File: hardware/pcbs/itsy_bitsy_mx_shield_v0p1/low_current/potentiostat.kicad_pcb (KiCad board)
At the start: 2 copper layers, 144.8 x 88.9 mm, 139 parts, among them K1 Conn_01x03, P1 Conn_01x02, P10 Conn_01x02, P11 Conn_01x02, P12 Conn_01x02, P13 Conn_02x05_Odd_Even, P14 Conn_02x05_Odd_Even, P15 Conn_02x02_Odd_Even, P16 Conn_02x02_Odd_Even, P17 Conn_01x02, P18 Conn_01x02, P19 Conn_01x02, P2 Conn_01x02, P20 Conn_01x02, P21 Conn_01x02, P22 Conn_01x02, P3 Conn_01x02, P4 Conn_01x02, P5 Conn_01x02, P6 Conn_01x02, P7 Conn_01x02, P8 Conn_01x02, P9 Conn_01x02, U1 74HC138, U11 OP07, U12 OP07, U13 OP07, U14 OP07, U15 OP07, U16 OP07, U17 OP07, U18 OP07, U19 74HC138, U2 ITSY_BITSY_M4, U20 OP07, U21 74HC138, U3 DG411xY, U4 DG411xY, U5 DG411xY, U6 MEA1D05XXSC, U7 DG411xY, U8 DG411xY, U9 TL072

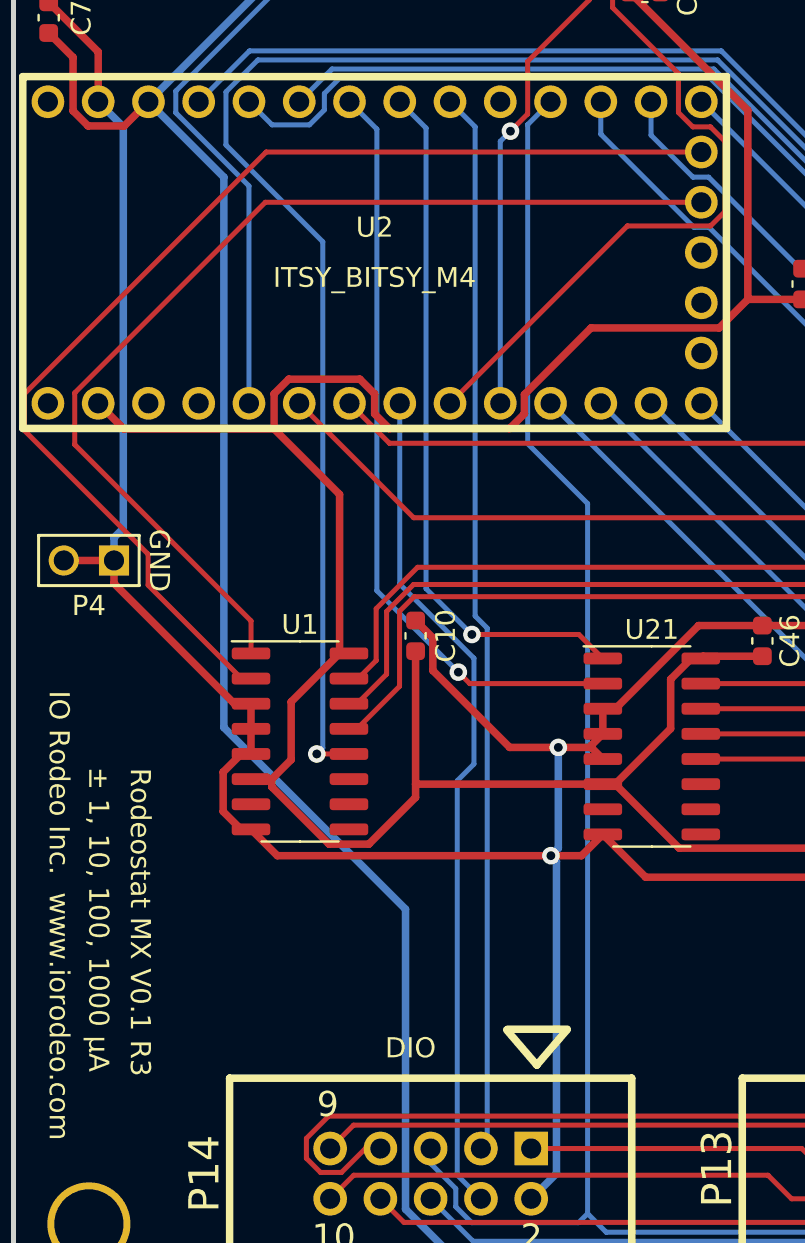
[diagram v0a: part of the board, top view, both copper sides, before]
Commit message: Added fab files to include through hole assembly.
Increased revision number V0.1 R4.  Remade gerbers to include addtional
elements on silkscreen.
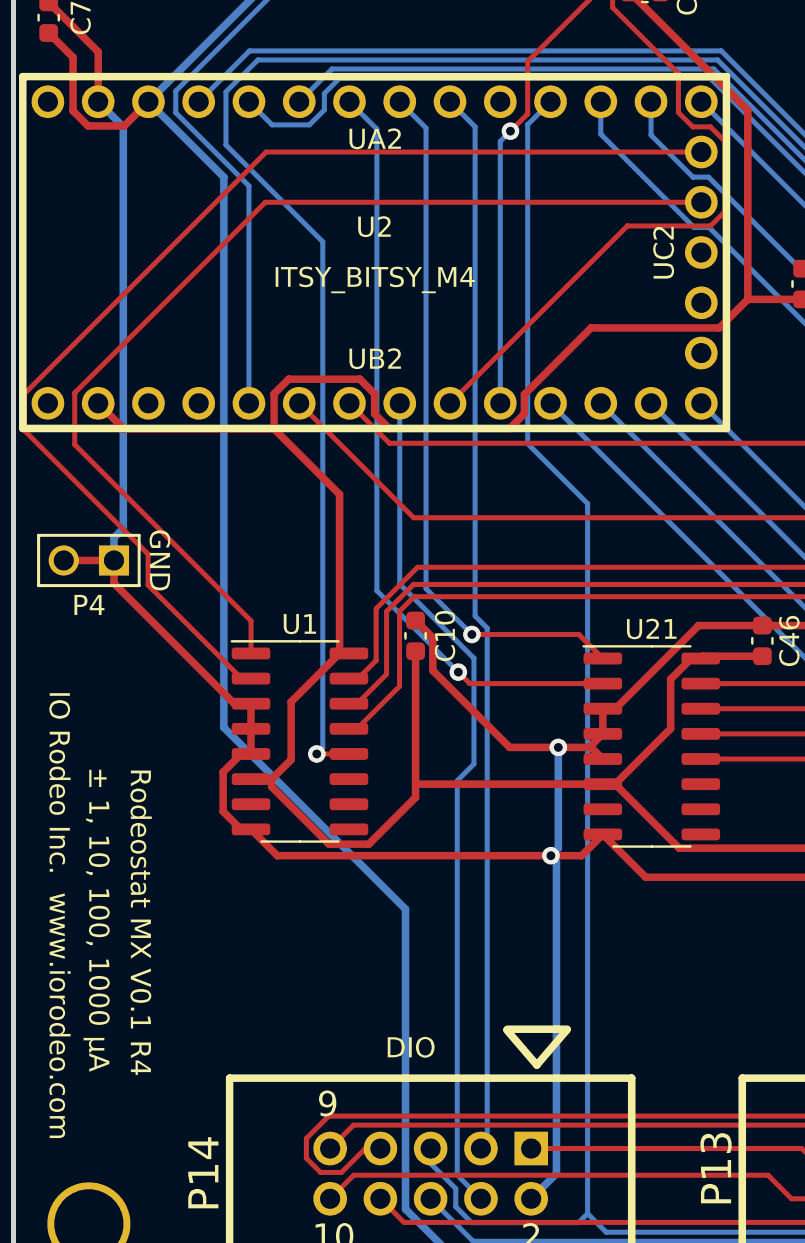
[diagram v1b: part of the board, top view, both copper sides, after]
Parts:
- added UA2: header_14_pos, dummy:header_14_pos, F.Cu at (69.0, 79.2)
- added UB2: header_14_pos, dummy:header_14_pos, F.Cu at (69.0, 94.4)
- added UC2: header_5_pos, dummy:header_5_pos, F.Cu at (85.6, 86.8)
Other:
- board text added: "Rodeostat MX V0.1 R4"
- board text removed: "Rodeostat MX V0.1 R3"
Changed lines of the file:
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@@
     (tracks 1443)
     (zones 0)
-    (modules 139)
+    (modules 142)
     (nets 133)
   )
@@
     (46 B.CrtYd user)
     (47 F.CrtYd user)
+    (49 F.Fab user)
   )
   (setup
@@
       (drillshape 0)
       (scaleselection 1)
-      (outputdirectory "gerber_v0p1_r3/"))
+      (outputdirectory "gerber_v0p1_r4/"))
   )
   (net 0 "")
@@
     (descr "Connecteur 3 pins")
     (tags "CONN DEV")
+    (attr smd)
     (fp_text reference K1 (at 5.08 -0.254 270) (layer F.SilkS)
       (effects (font (size 1.016 1.016) (thickness 0.2032)))
@@
   (module 5x2_shrd_header:5X2_SHRD_HEADER (layer F.Cu)
     (at 71.882 133.35 180)
+    (attr smd)
     (fp_text reference P14 (at 11.43 0 270) (layer F.SilkS)
       (effects (font (size 1.524 1.524) (thickness 0.3048)))
@@
   (module 5x2_shrd_header:5X2_SHRD_HEADER (layer F.Cu)
     (at 97.79 133.35 180)
+    (attr smd)
     (fp_text reference P13 (at 11.43 0.254 270) (layer F.SilkS)
       (effects (font (size 1.524 1.524) (thickness 0.3048)))
@@
     (descr "Double rangee de contacts 2 x 2 pins")
     (tags CONN)
+    (attr smd)
     (fp_text reference P16 (at -3.556 0 90) (layer F.SilkS)
       (effects (font (size 1.016 1.016) (thickness 0.2032)))
@@
     (descr "Double rangee de contacts 2 x 2 pins")
     (tags CONN)
+    (attr smd)
     (fp_text reference P15 (at -3.556 0 90) (layer F.SilkS)
       (effects (font (size 1.016 1.016) (thickness 0.2032)))
@@
   (module MEA1:MEA1 (layer F.Cu)
     (at 70.358 54.102)
+    (attr smd)
     (fp_text reference U6 (at -9.652 1.016 90) (layer F.SilkS)
       (effects (font (size 1.016 1.016) (thickness 0.2032)))
@@
   (module ost_connblocks:CONNBLOCK2 (layer F.Cu)
     (at 189.23 71.12 270)
+    (attr smd)
     (fp_text reference P1 (at 0.508 4.826 90) (layer F.SilkS)
       (effects (font (size 1.524 1.524) (thickness 0.3048)))
@@
   (module ost_connblocks:CONNBLOCK2 (layer F.Cu)
     (at 189.23 82.55 270)
+    (attr smd)
     (fp_text reference P2 (at 0.508 4.826 90) (layer F.SilkS)
       (effects (font (size 1.524 1.524) (thickness 0.3048)))
@@
   (module ost_connblocks:CONNBLOCK2 (layer F.Cu)
     (at 189.23 93.98 270)
+    (attr smd)
     (fp_text reference P3 (at 0.508 4.826 90) (layer F.SilkS)
       (effects (font (size 1.524 1.524) (thickness 0.3048)))
@@
       (net 10 /GND))
   )
+  (module dummy:header_14_pos (layer F.Cu)
+    (at 69.05 79.179999)
+    (attr smd)
+    (fp_text reference UA2 (at 0.038 1.909501) (layer F.SilkS)
+      (effects (font (size 1.016 1.016) (thickness 0.2032)))
+    )
+    (fp_text value header_14_pos (at 0.127 -1.651) (layer F.Fab) hide
+      (effects (font (size 1 1) (thickness 0.15)))
+    )
+    (fp_circle (center 16.51 0) (end 17.018 0) (layer F.Fab) (width 0.15))
+    (fp_circle (center 13.97 0) (end 14.478 0) (layer F.Fab) (width 0.15))
+    (fp_circle (center 11.43 0) (end 11.938 0) (layer F.Fab) (width 0.15))
+    (fp_circle (center 8.89 0) (end 9.398 0) (layer F.Fab) (width 0.15))
+    (fp_circle (center -16.51 0) (end -16.002 0) (layer F.Fab) (width 0.15))
+    (fp_circle (center -13.97 0) (end -13.462 0) (layer F.Fab) (width 0.15))
+    (fp_circle (center -11.43 0) (end -10.922 0) (layer F.Fab) (width 0.15))
+    (fp_circle (center -8.89 0) (end -8.382 0) (layer F.Fab) (width 0.15))
+    (fp_circle (center 6.35 0) (end 6.858 0) (layer F.Fab) (width 0.15))
+    (fp_circle (center -6.35 0) (end -5.842 0) (layer F.Fab) (width 0.15))
+    (fp_circle (center 3.81 0) (end 4.318 0) (layer F.Fab) (width 0.15))
+    (fp_circle (center 1.27 0) (end 1.778 0) (layer F.Fab) (width 0.15))
+    (fp_circle (center -3.81 0) (end -3.302 0) (layer F.Fab) (width 0.15))
+    (fp_circle (center -1.27 0) (end -0.762 0) (layer F.Fab) (width 0.15))
+  )
+  (module dummy:header_14_pos (layer F.Cu)
+    (at 69.05 94.41942)
+    (attr smd)
+    (fp_text reference UB2 (at 0.038 -2.21742) (layer F.SilkS)
+      (effects (font (size 1.016 1.016) (thickness 0.2032)))
+    )
+    (fp_text value header_14_pos (at 0.127 -1.651) (layer F.Fab) hide
+      (effects (font (size 1 1) (thickness 0.15)))
+    )
+    (fp_circle (center -1.27 0) (end -0.762 0) (layer F.Fab) (width 0.15))
+    (fp_circle (center -3.81 0) (end -3.302 0) (layer F.Fab) (width 0.15))
+    (fp_circle (center 1.27 0) (end 1.778 0) (layer F.Fab) (width 0.15))
+    (fp_circle (center 3.81 0) (end 4.318 0) (layer F.Fab) (width 0.15))
+    (fp_circle (center -6.35 0) (end -5.842 0) (layer F.Fab) (width 0.15))
+    (fp_circle (center 6.35 0) (end 6.858 0) (layer F.Fab) (width 0.15))
+    (fp_circle (center -8.89 0) (end -8.382 0) (layer F.Fab) (width 0.15))
+    (fp_circle (center -11.43 0) (end -10.922 0) (layer F.Fab) (width 0.15))
+    (fp_circle (center -13.97 0) (end -13.462 0) (layer F.Fab) (width 0.15))
+    (fp_circle (center -16.51 0) (end -16.002 0) (layer F.Fab) (width 0.15))
+    (fp_circle (center 8.89 0) (end 9.398 0) (layer F.Fab) (width 0.15))
+    (fp_circle (center 11.43 0) (end 11.938 0) (layer F.Fab) (width 0.15))
+    (fp_circle (center 13.97 0) (end 14.478 0) (layer F.Fab) (width 0.15))
+    (fp_circle (center 16.51 0) (end 17.018 0) (layer F.Fab) (width 0.15))
+  )
+  (module dummy:header_5_pos (layer F.Cu)
+    (at 85.5599 86.8 270)
+    (attr smd)
+    (fp_text reference UC2 (at 0 1.8669 90) (layer F.SilkS)
+      (effects (font (size 1.016 1.016) (thickness 0.2032)))
+    )
+    (fp_text value header_5_pos (at 0 -1.397 90) (layer F.Fab) hide
+      (effects (font (size 1 1) (thickness 0.15)))
+    )
+    (fp_circle (center 0 0) (end 0.508 0) (layer F.Fab) (width 0.15))
+    (fp_circle (center -2.54 0) (end -2.032 0) (layer F.Fab) (width 0.15))
+    (fp_circle (center -5.08 0) (end -4.572 0) (layer F.Fab) (width 0.15))
+    (fp_circle (center 2.54 0) (end 3.048 0) (layer F.Fab) (width 0.15))
+    (fp_circle (center 5.08 0) (end 5.588 0) (layer F.Fab) (width 0.15))
+  )
   (gr_text "± 1, 10, 100, 1000 μA" (at 55.1 120.5 270) (layer F.SilkS)
     (effects (font (size 1.016 1.016) (thickness 0.2032)))
@@
     (effects (font (size 1.016 1.016) (thickness 0.2032)))
   )
-  (gr_text "Rodeostat MX V0.1 R3" (at 57.2 120.642 270) (layer F.SilkS)
+  (gr_text "Rodeostat MX V0.1 R4" (at 57.2 120.642 270) (layer F.SilkS)
     (effects (font (size 1.016 1.016) (thickness 0.2032)))
   )
